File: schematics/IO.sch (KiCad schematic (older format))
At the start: 80 parts, among them J4 Outputs, J8 Power Pins, Q1 MMBT3906, U10 TL082, U11 6S21, U12 6S21, U13 TL082, U16 TL082, U6 DS1307Z+, U7 LM324, U8 TL082, U9 MCP4728, X2 32.768 kHz

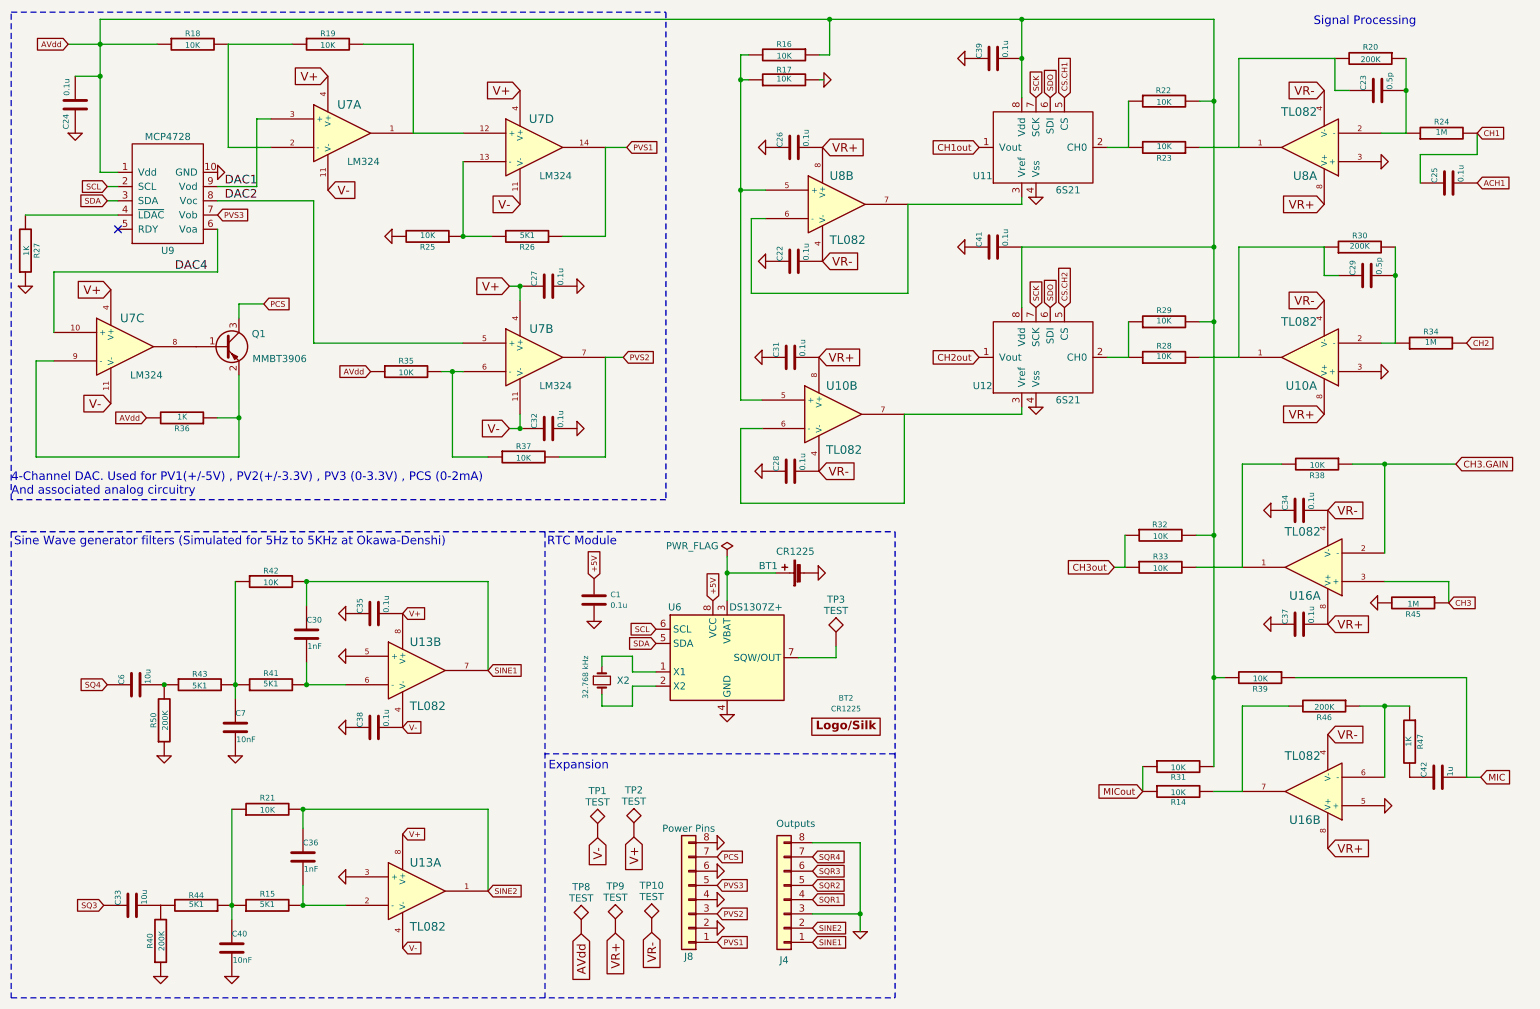
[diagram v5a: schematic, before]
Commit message: refactor: corrected IC annotation order
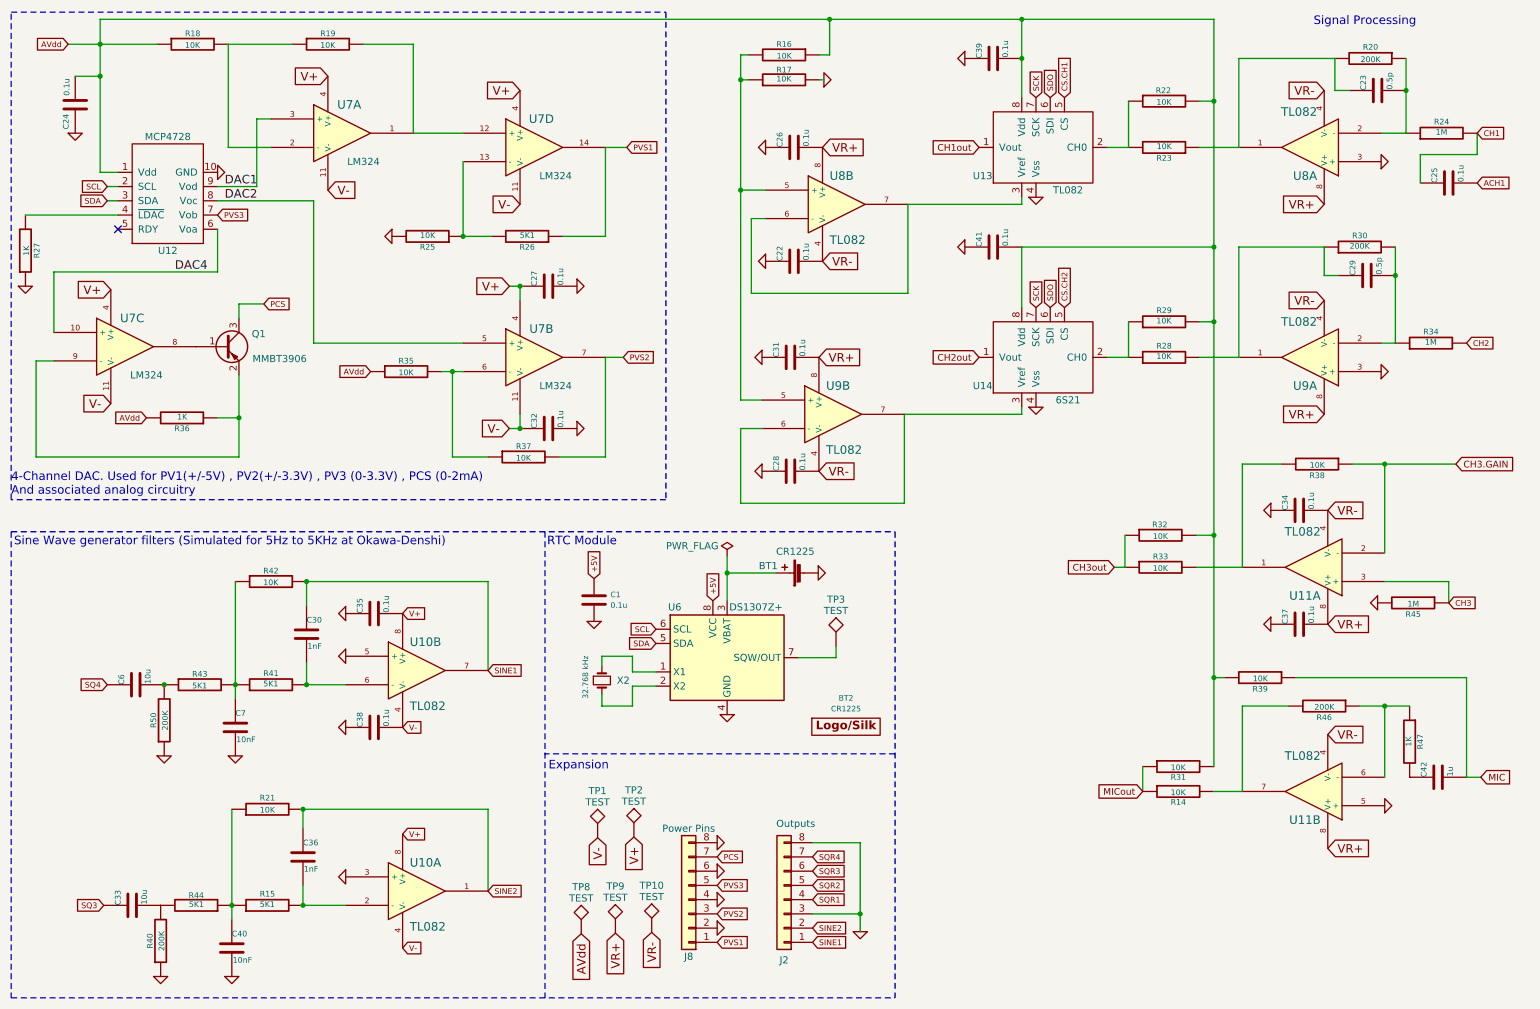
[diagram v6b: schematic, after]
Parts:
- U10, U12, U13, U16, U8: footprint Housings_SOIC:SOIC-8_3.9x4.9mm_Pitch1.27mm -> Package_SO:SOIC-8_3.9x4.9mm_P1.27mm
- U11: value 6S21 -> TL082; footprint Housings_SOIC:SOIC-8_3.9x4.9mm_Pitch1.27mm -> Package_SO:SOIC-8_3.9x4.9mm_P1.27mm
- U12: renamed from U9; footprint Housings_SSOP:MSOP-10_3x3mm_Pitch0.5mm -> Package_SO:MSOP-10_3x3mm_P0.5mm
- U7: footprint Housings_SOIC:SOIC-14_3.9x8.7mm_Pitch1.27mm -> Package_SO:SOIC-14_3.9x8.7mm_P1.27mm
- renumbered J4 to J2
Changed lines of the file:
@@
 P 9675 2950
 AR Path="/5446FCD7" Ref="U10"  Part="1"
-AR Path="/54260FB5/5446FCD7" Ref="U10"  Part="1"
-F 0 "U10" H 9625 3150 60  0000 L CNN
+AR Path="/54260FB5/5446FCD7" Ref="U9"  Part="1"
+F 0 "U9" H 9625 3150 60  0000 L CNN
 F 1 "TL082" H 9625 2700 60  0000 L CNN
-F 2 "Housings_SOIC:SOIC-8_3.9x4.9mm_Pitch1.27mm" H 9675 2950 60  0001 C CNN
+F 2 "Package_SO:SOIC-8_3.9x4.9mm_P1.27mm" H 9675 2950 60  0001 C CNN
 F 3 "http://www.ti.com/general/docs/suppproductinfo.tsp?distId=26&gotoUrl=http%3A%2F%2Fwww.ti.com%2Flit%2Fgpn%2Ftl082" H 9675 2950 60  0001 C CNN
 F 4 "SOIC 8" H 9675 2950 50  0001 C CNN "Description"
@@
 P 6325 3350
 AR Path="/54471802" Ref="U10"  Part="2"
-AR Path="/54260FB5/54471802" Ref="U10"  Part="2"
-F 0 "U10" H 6275 3550 60  0000 L CNN
+AR Path="/54260FB5/54471802" Ref="U9"  Part="2"
+F 0 "U9" H 6275 3550 60  0000 L CNN
 F 1 "TL082" H 6275 3100 60  0000 L CNN
-F 2 "Housings_SOIC:SOIC-8_3.9x4.9mm_Pitch1.27mm" H 6325 3350 60  0001 C CNN
+F 2 "Package_SO:SOIC-8_3.9x4.9mm_P1.27mm" H 6325 3350 60  0001 C CNN
 F 3 "http://www.ti.com/general/docs/suppproductinfo.tsp?distId=26&gotoUrl=http%3A%2F%2Fwww.ti.com%2Flit%2Fgpn%2Ftl082" H 6325 3350 60  0001 C CNN
 F 4 "SOIC 8" H 6325 3350 50  0001 C CNN "Description"
@@
 F 0 "U7" H 4275 1675 60  0000 C CNN
 F 1 "LM324" H 4375 1275 50  0000 C CNN
-F 2 "Housings_SOIC:SOIC-14_3.9x8.7mm_Pitch1.27mm" H 4225 1475 60  0001 C CNN
+F 2 "Package_SO:SOIC-14_3.9x8.7mm_P1.27mm" H 4225 1475 60  0001 C CNN
 F 3 "http://www.ti.com/general/docs/suppproductinfo.tsp?distId=26&gotoUrl=http%3A%2F%2Fwww.ti.com%2Flit%2Fgpn%2FLM324" H 4225 1475 60  0001 C CNN
 F 4 "SOIC 14" H 4225 1475 50  0001 C CNN "Description"
@@
 F 0 "U7" H 1400 3075 60  0000 C CNN
 F 1 "LM324" H 1500 2675 50  0000 C CNN
-F 2 "Housings_SOIC:SOIC-14_3.9x8.7mm_Pitch1.27mm" H 1350 2875 60  0001 C CNN
+F 2 "Package_SO:SOIC-14_3.9x8.7mm_P1.27mm" H 1350 2875 60  0001 C CNN
 F 3 "http://www.ti.com/general/docs/suppproductinfo.tsp?distId=26&gotoUrl=http%3A%2F%2Fwww.ti.com%2Flit%2Fgpn%2FLM324" H 1350 2875 60  0001 C CNN
 F 4 "SOIC 14" H 1350 2875 50  0001 C CNN "Description"
@@
 F 0 "U7" H 2925 1575 60  0000 C CNN
 F 1 "LM324" H 3025 1175 50  0000 C CNN
-F 2 "Housings_SOIC:SOIC-14_3.9x8.7mm_Pitch1.27mm" H 2875 1375 60  0001 C CNN
+F 2 "Package_SO:SOIC-14_3.9x8.7mm_P1.27mm" H 2875 1375 60  0001 C CNN
 F 3 "http://www.ti.com/general/docs/suppproductinfo.tsp?distId=26&gotoUrl=http%3A%2F%2Fwww.ti.com%2Flit%2Fgpn%2FLM324" H 2875 1375 60  0001 C CNN
 F 4 "SOIC 14" H 2875 1375 50  0001 C CNN "Description"
@@
 F 0 "U7" H 4275 3150 60  0000 C CNN
 F 1 "LM324" H 4375 2750 50  0000 C CNN
-F 2 "Housings_SOIC:SOIC-14_3.9x8.7mm_Pitch1.27mm" H 4225 2950 60  0001 C CNN
+F 2 "Package_SO:SOIC-14_3.9x8.7mm_P1.27mm" H 4225 2950 60  0001 C CNN
 F 3 "http://www.ti.com/general/docs/suppproductinfo.tsp?distId=26&gotoUrl=http%3A%2F%2Fwww.ti.com%2Flit%2Fgpn%2FLM324" H 4225 2950 60  0001 C CNN
 F 4 "SOIC 14" H 4225 2950 50  0001 C CNN "Description"
@@
 $EndComp
 $Comp
-L PSLab:MCP4728-RESCUE-PSLab U9
+L PSLab:MCP4728-RESCUE-PSLab U12
 U 1 1 555FFB01
 P 1650 1800
-F 0 "U9" H 1650 1400 50  0000 C CNN
+F 0 "U12" H 1650 1400 50  0000 C CNN
 F 1 "MCP4728" H 1650 2200 50  0000 C CNN
-F 2 "Housings_SSOP:MSOP-10_3x3mm_Pitch0.5mm" H 1650 1800 50  0001 C CNN
-F 3 "https://eu.mouser.com/datasheet/2/268/22187E-12972.pdf" H 1650 1800 50  0001 C CNN
+F 2 "Package_SO:MSOP-10_3x3mm_P0.5mm" H 1650 1800 50  0001 C CNN
+F 3 "http://www.ti.com/general/docs/suppproductinfo.tsp?distId=26&gotoUrl=http%3A%2F%2Fwww.ti.com%2Flit%2Fgpn%2Ftl082" H 1650 1800 50  0001 C CNN
 F 4 "MSOP 10" H 1650 1800 50  0001 C CNN "Description"
 F 5 "MCP4728-E/UN" H 1650 1800 50  0001 C CNN "Mfr No."
@@
 F 0 "U8" H 9625 1675 60  0000 L CNN
 F 1 "TL082" H 9625 1225 60  0000 L CNN
-F 2 "Housings_SOIC:SOIC-8_3.9x4.9mm_Pitch1.27mm" H 9675 1475 60  0001 C CNN
+F 2 "Package_SO:SOIC-8_3.9x4.9mm_P1.27mm" H 9675 1475 60  0001 C CNN
 F 3 "http://www.ti.com/general/docs/suppproductinfo.tsp?distId=26&gotoUrl=http%3A%2F%2Fwww.ti.com%2Flit%2Fgpn%2Ftl082" H 9675 1475 60  0001 C CNN
 F 4 "SOIC 8" H 9675 1475 50  0001 C CNN "Description"
@@
 F 0 "U8" H 6300 2075 60  0000 L CNN
 F 1 "TL082" H 6300 1625 60  0000 L CNN
-F 2 "Housings_SOIC:SOIC-8_3.9x4.9mm_Pitch1.27mm" H 6350 1875 60  0001 C CNN
+F 2 "Package_SO:SOIC-8_3.9x4.9mm_P1.27mm" H 6350 1875 60  0001 C CNN
 F 3 "http://www.ti.com/general/docs/suppproductinfo.tsp?distId=26&gotoUrl=http%3A%2F%2Fwww.ti.com%2Flit%2Fgpn%2Ftl082" H 6350 1875 60  0001 C CNN
 F 4 "SOIC 8" H 6350 1875 50  0001 C CNN "Description"
@@
 P 3400 5150
 AR Path="/55C273D0" Ref="U13"  Part="2"
-AR Path="/54260FB5/55C273D0" Ref="U13"  Part="2"
-F 0 "U13" H 3350 5350 60  0000 L CNN
+AR Path="/54260FB5/55C273D0" Ref="U10"  Part="2"
+F 0 "U10" H 3350 5350 60  0000 L CNN
 F 1 "TL082" H 3350 4900 60  0000 L CNN
-F 2 "Housings_SOIC:SOIC-8_3.9x4.9mm_Pitch1.27mm" H 3400 5150 60  0001 C CNN
+F 2 "Package_SO:SOIC-8_3.9x4.9mm_P1.27mm" H 3400 5150 60  0001 C CNN
 F 3 "http://www.ti.com/general/docs/suppproductinfo.tsp?distId=26&gotoUrl=http%3A%2F%2Fwww.ti.com%2Flit%2Fgpn%2Ftl082" H 3400 5150 60  0001 C CNN
 F 4 "SOIC 8" H 3400 5150 50  0001 C CNN "Description"
@@
 P 3400 6700
 AR Path="/55C276F1" Ref="U13"  Part="1"
-AR Path="/54260FB5/55C276F1" Ref="U13"  Part="1"
-F 0 "U13" H 3350 6900 60  0000 L CNN
+AR Path="/54260FB5/55C276F1" Ref="U10"  Part="1"
+F 0 "U10" H 3350 6900 60  0000 L CNN
 F 1 "TL082" H 3350 6450 60  0000 L CNN
-F 2 "Housings_SOIC:SOIC-8_3.9x4.9mm_Pitch1.27mm" H 3400 6700 60  0001 C CNN
+F 2 "Package_SO:SOIC-8_3.9x4.9mm_P1.27mm" H 3400 6700 60  0001 C CNN
 F 3 "http://www.ti.com/general/docs/suppproductinfo.tsp?distId=26&gotoUrl=http%3A%2F%2Fwww.ti.com%2Flit%2Fgpn%2Ftl082" H 3400 6700 60  0001 C CNN
 F 4 "SOIC 8" H 3400 6700 50  0001 C CNN "Description"
@@
 P 7800 1475
 AR Path="/55E941B6" Ref="U11"  Part="1"
-AR Path="/54260FB5/55E941B6" Ref="U11"  Part="1"
-F 0 "U11" H 7375 1275 50  0000 C CNN
-F 1 "6S21" H 7975 1175 50  0000 C CNN
-F 2 "Housings_SOIC:SOIC-8_3.9x4.9mm_Pitch1.27mm" H 7950 1275 50  0001 C CNN
-F 3 "https://eu.mouser.com/datasheet/2/268/21117a-70287.pdf" H 7800 1875 50  0001 C CNN
+AR Path="/54260FB5/55E941B6" Ref="U13"  Part="1"
+F 0 "U13" H 7375 1275 50  0000 C CNN
+F 1 "TL082" H 7975 1175 50  0000 C CNN
+F 2 "Package_SO:SOIC-8_3.9x4.9mm_P1.27mm" H 7950 1275 50  0001 C CNN
+F 3 "http://www.ti.com/general/docs/suppproductinfo.tsp?distId=26&gotoUrl=http%3A%2F%2Fwww.ti.com%2Flit%2Fgpn%2Ftl082" H 7800 1875 50  0001 C CNN
 F 4 "SOIC 8" H 7800 1475 50  0001 C CNN "Description"
 F 5 "MCP6S21-I/SN" H 7800 1475 50  0001 C CNN "Mfr No."
@@
 P 7800 2950
 AR Path="/55E9B36E" Ref="U12"  Part="1"
-AR Path="/54260FB5/55E9B36E" Ref="U12"  Part="1"
-F 0 "U12" H 7375 2750 50  0000 C CNN
+AR Path="/54260FB5/55E9B36E" Ref="U14"  Part="1"
+F 0 "U14" H 7375 2750 50  0000 C CNN
 F 1 "6S21" H 7975 2650 50  0000 C CNN
-F 2 "Housings_SOIC:SOIC-8_3.9x4.9mm_Pitch1.27mm" H 7950 2750 50  0001 C CNN
+F 2 "Package_SO:SOIC-8_3.9x4.9mm_P1.27mm" H 7950 2750 50  0001 C CNN
 F 3 "https://eu.mouser.com/datasheet/2/268/21117a-70287.pdf" H 7800 3350 50  0001 C CNN
 F 4 "SOIC 8" H 7800 2950 50  0001 C CNN "Description"
@@
 P 9700 4425
 AR Path="/55B8CB26" Ref="U16"  Part="1"
-AR Path="/54260FB5/55B8CB26" Ref="U16"  Part="1"
-F 0 "U16" H 9650 4625 60  0000 L CNN
+AR Path="/54260FB5/55B8CB26" Ref="U11"  Part="1"
+F 0 "U11" H 9650 4625 60  0000 L CNN
 F 1 "TL082" H 9650 4175 60  0000 L CNN
-F 2 "Housings_SOIC:SOIC-8_3.9x4.9mm_Pitch1.27mm" H 9700 4425 60  0001 C CNN
+F 2 "Package_SO:SOIC-8_3.9x4.9mm_P1.27mm" H 9700 4425 60  0001 C CNN
 F 3 "http://www.ti.com/general/docs/suppproductinfo.tsp?distId=26&gotoUrl=http%3A%2F%2Fwww.ti.com%2Flit%2Fgpn%2Ftl082" H 9700 4425 60  0001 C CNN
 F 4 "SOIC 8" H 9700 4425 50  0001 C CNN "Description"
@@
 P 9700 6000
 AR Path="/55B8CB3C" Ref="U16"  Part="2"
-AR Path="/54260FB5/55B8CB3C" Ref="U16"  Part="2"
-F 0 "U16" H 9650 6200 60  0000 L CNN
+AR Path="/54260FB5/55B8CB3C" Ref="U11"  Part="2"
+F 0 "U11" H 9650 6200 60  0000 L CNN
 F 1 "TL082" H 9650 5750 60  0000 L CNN
-F 2 "Housings_SOIC:SOIC-8_3.9x4.9mm_Pitch1.27mm" H 9700 6000 60  0001 C CNN
+F 2 "Package_SO:SOIC-8_3.9x4.9mm_P1.27mm" H 9700 6000 60  0001 C CNN
 F 3 "http://www.ti.com/general/docs/suppproductinfo.tsp?distId=26&gotoUrl=http%3A%2F%2Fwww.ti.com%2Flit%2Fgpn%2Ftl082" H 9700 6000 60  0001 C CNN
 F 4 "SOIC 8" H 9700 6000 50  0001 C CNN "Description"
@@
 $EndComp
 $Comp
-L Connector_Generic:Conn_01x08 J4
+L Connector_Generic:Conn_01x08 J2
 U 1 1 5EF10C2C
 P 5980 6760
-F 0 "J4" H 5980 7185 50  0000 C CNN
+F 0 "J2" H 5980 7185 50  0000 C CNN
 F 1 "Outputs" H 5898 6226 50  0000 C CNN
 F 2 "Connector_PinSocket_2.54mm:PinSocket_1x08_P2.54mm_Vertical" H 5980 6760 50  0001 C CNN
